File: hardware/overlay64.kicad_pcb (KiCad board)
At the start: 2 copper layers, 54 x 43.2 mm, 15 parts, among them IC1 ATMEGA328P-P, P1 ISP, P2 VIC IN, P3 VIC OUT, Q1 NPN, U1 LM1881, Y1 16MHz

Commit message: Hardware: Removed VIC-Sockets and pcb layout
Designing this as a VIC-Adpater-board is too complicated, and maybe
not possible (depending on what the modulator still does to the signal
to make it a proper C/Y signal).

It's probably simpler to get LUMA from the connector internally.
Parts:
- removed C1, C2: 18pF, Capacitors_ThroughHole:C_Disc_D3_P2.5
- removed C3, C4, C5, C6: 100nF, Capacitors_ThroughHole:C_Disc_D3_P2.5
- removed IC1: ATMEGA328P-P, Housings_DIP:DIP-28_W7.62mm
- removed P1: ISP, Pin_Headers:Pin_Header_Straight_2x03
- removed P2: VIC IN, Housings_DIP:DIP-40_W15.24mm
- removed P3: VIC OUT, Housings_DIP:DIP-40_W15.24mm
- removed Q1: NPN, TO_SOT_Packages_THT:TO-92_Inline_Narrow_Oval
- removed R1: 680k, Discret:R1
- removed RV1: 1k, Potentiometers:Potentiometer_Bourns_3339H_Angular_ScrewUp
- removed U1: LM1881, Housings_DIP:DIP-8_W7.62mm
- removed Y1: 16MHz, Crystals:Crystal_HC49-U_Vertical
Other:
- board outline removed

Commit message: Hardware: First draft of pcb layout (rough)
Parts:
- added C1: 18pF, Capacitors_ThroughHole:C_Disc_D3_P2.5, F.Cu at (135.9, 95.9)
- added C2: 18pF, Capacitors_ThroughHole:C_Disc_D3_P2.5, F.Cu at (135.9, 106.0)
- added C3: 100nF, Capacitors_ThroughHole:C_Disc_D3_P2.5, F.Cu at (141.0, 93.3)
- added C4: 100nF, Capacitors_ThroughHole:C_Disc_D3_P2.5, F.Cu at (138.4, 79.4)
- added C5: 100nF, Capacitors_ThroughHole:C_Disc_D3_P2.5, F.Cu at (132.1, 102.2)
- added C6: 100nF, Capacitors_ThroughHole:C_Disc_D3_P2.5, F.Cu at (141.0, 84.5)
- added IC1: ATMEGA328P-P, Housings_DIP:DIP-28_W7.62mm, F.Cu at (143.5, 79.4)
- added JP1: BACKDROP, Pin_Headers:Pin_Header_Straight_1x02, F.Cu at (129.5, 102.2)
- added P1: ISP, Pin_Headers:Pin_Header_Straight_2x03, F.Cu at (134.6, 112.4)
- added P2: MAIN, Pin_Headers:Pin_Header_Straight_1x03, F.Cu at (129.5, 111.1)
- added P3: INPUT/BYPASS, Pin_Headers:Pin_Header_Straight_2x14, F.Cu at (154.9, 79.4)
- added Q1: BC547B, TO_SOT_Packages_THT:TO-92_Inline_Narrow_Oval, F.Cu at (139.7, 87.0)
- added R1: 680k, Discret:R1, F.Cu at (138.4, 83.2)
- added R2: 4k7, Discret:R1, F.Cu at (135.9, 92.1)
- added RV1: 1k, Potentiometers:Potentiometer_Bourns_3339P_Angular_ScrewUp, F.Cu at (128.3, 93.3)
- added U1: LM1881, Housings_DIP:DIP-8_W7.62mm, F.Cu at (128.3, 79.4)
- added Y1: 20MHz, Crystals:Crystal_HC49-U_Vertical, F.Cu at (139.7, 101.0)
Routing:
- net GND: track 0.00 -> 76.5 mm
- net VCC: track 0.00 -> 72.4 mm
- net /IN1: track 0.00 -> 64.4 mm, vias 0 -> 1
- net /~RESET: track 0.00 -> 56.5 mm, vias 0 -> 1
- net /MOSI: track 0.00 -> 49.9 mm
- net /IN0: track 0.00 -> 44.7 mm
- net /IN8: track 0.00 -> 26.1 mm
- net /IN9: track 0.00 -> 25.8 mm
- net /IN7: track 0.00 -> 24.3 mm
- net /IN10: track 0.00 -> 24.1 mm
- net /MISO: track 0.00 -> 23.4 mm
- net /SCK: track 0.00 -> 21.9 mm
- net Net-(C5-Pad2): track 0.00 -> 20.1 mm
- net Net-(IC1-Pad4): track 0.00 -> 19.9 mm
- net Net-(JP1-Pad2): track 0.00 -> 18.8 mm
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- added copper zone on B.Cu, net GND
- added copper zone on F.Cu, net GND
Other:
- board outline added: 31.8 x 35.6 mm
- net class Default: via_dia 0.6 -> 1
- net class Power added: clearance 0.2, trace_width 0.5, via_dia 1, via_drill 0.4

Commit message: Hardware: Updated netlist to include OE/OR pins
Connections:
- IC1 pad 12: /IN12 -> /~OE
- IC1 pad 13: /~OE -> /~OR
- P3 pad 25: /IN12 -> /~OE
- P3 pad 26: /IN12 -> /~OE
- P3 pad 27: /~OE -> /~OR
- P3 pad 28: /~OE -> /~OR
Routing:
- net /IN12: track 15.0 -> 0.00 mm
- net /~OR: track 0.00 -> 15.0 mm

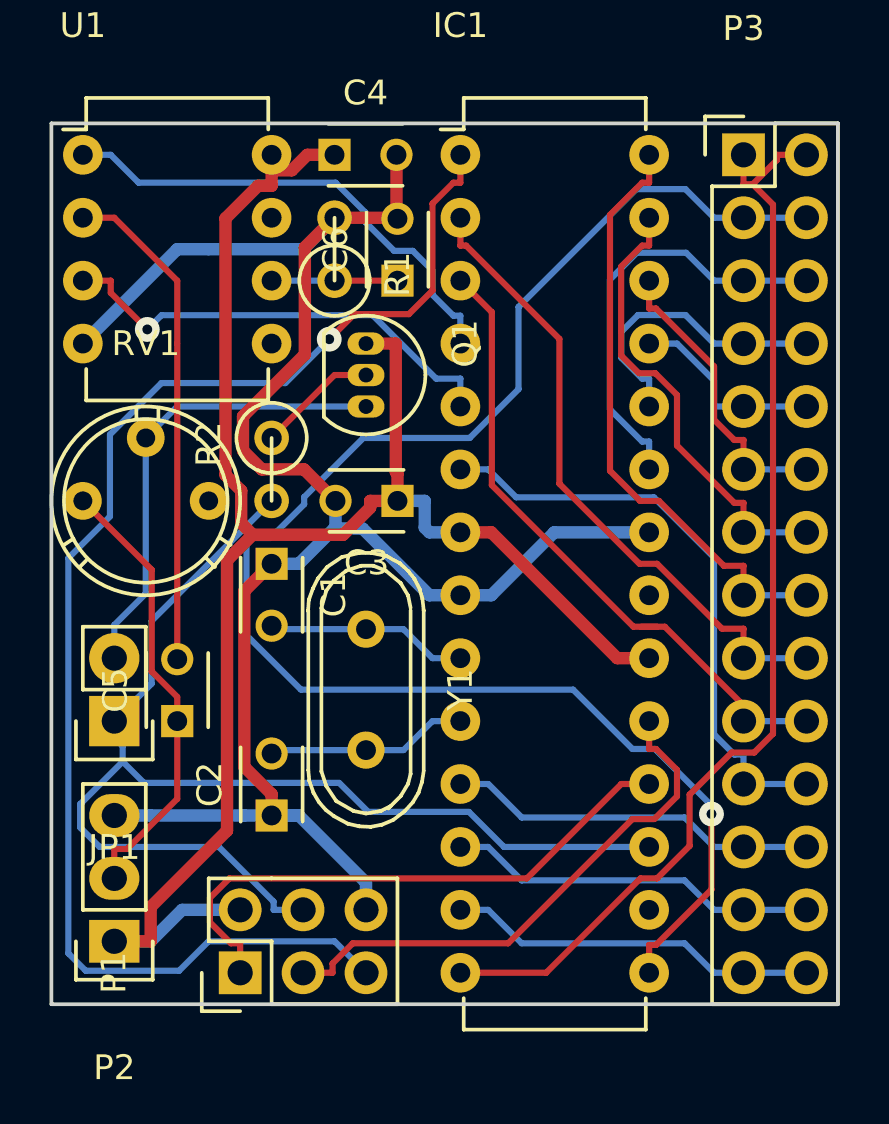
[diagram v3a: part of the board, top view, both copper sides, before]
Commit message: Hardware: Adjusted input pin connections to new logical layout
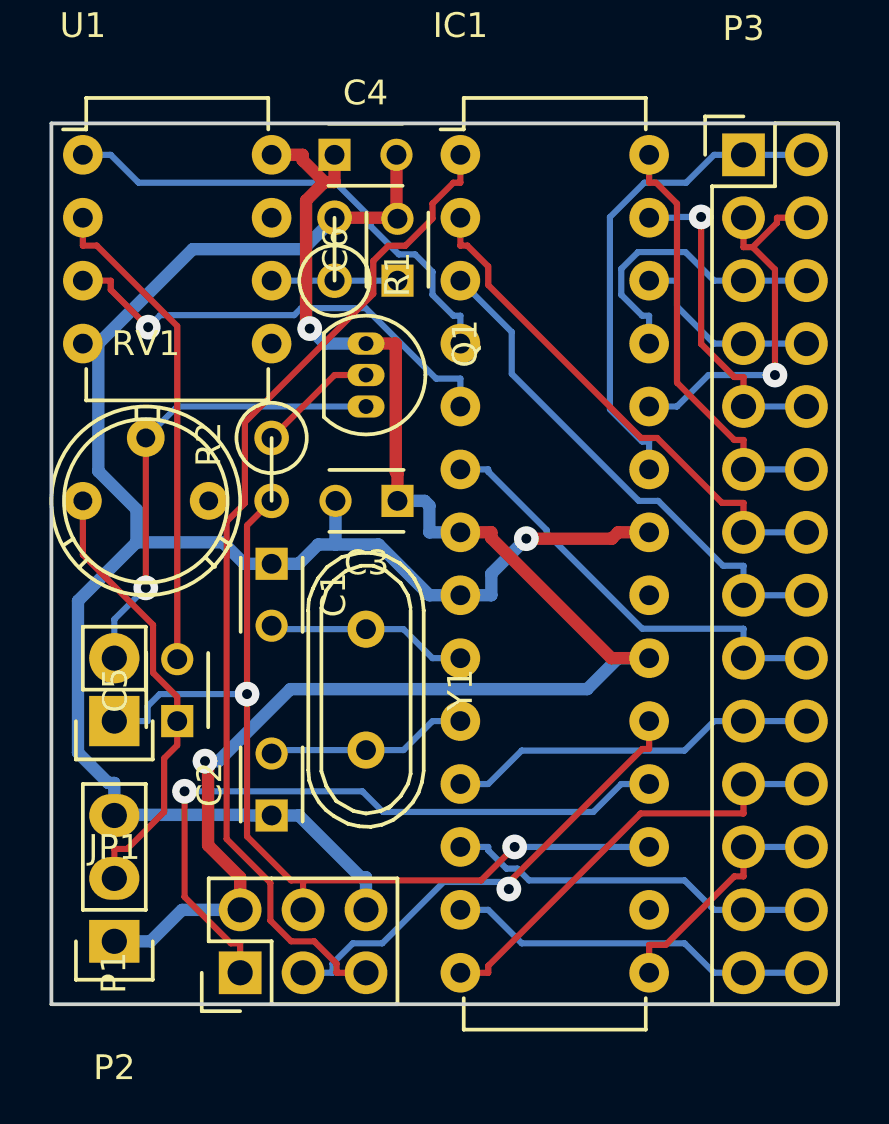
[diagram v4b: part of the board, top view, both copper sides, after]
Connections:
- IC1 pad 11: /IN11 -> /IN9
- IC1 pad 14: /IN0 -> /IN10
- IC1 pad 15: /IN1 -> /IN11
- IC1 pad 2: /IN8 -> /IN6
- IC1 pad 23: /IN2 -> /IN0
- IC1 pad 24: /IN3 -> /IN1
- IC1 pad 25: /IN4 -> /IN2
- IC1 pad 26: /IN5 -> /IN3
- IC1 pad 27: /IN6 -> /IN4
- IC1 pad 28: /IN7 -> /IN5
- IC1 pad 3: /IN9 -> /IN7
- IC1 pad 6: /IN10 -> /IN8
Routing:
- net /IN1: track 64.4 -> 15.5 mm
- net /IN0: track 44.7 -> 20.0 mm
- net /~RESET: track 56.5 -> 41.1 mm, vias 1 -> 0
- net /MOSI: track 49.9 -> 38.8 mm, vias 0 -> 2
- net /IN9: track 25.8 -> 15.0 mm
- net /IN8: track 26.1 -> 17.9 mm
- net VCC: track 72.4 -> 66.0 mm, vias 0 -> 2
- net /IN10: track 24.1 -> 18.0 mm
- net /IN2: track 17.3 -> 11.9 mm
- net /IN4: track 8.01 -> 13.2 mm, vias 0 -> 1
- net /IN11: track 15.0 -> 9.81 mm
- net /IN5: track 12.1 -> 17.2 mm
- net /MISO: track 23.4 -> 28.0 mm, vias 0 -> 1
- net /IN3: track 11.9 -> 8.01 mm
- net /IN7: track 24.3 -> 20.9 mm
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
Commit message: Hardware: Rearranged components, rerouting...
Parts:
- removed RV1: 1k, Potentiometers:Potentiometer_Bourns_3339P_Angular_ScrewUp
- added 1K: 1k, Potentiometers:Potentiometer_Bourns_3339P_Angular_ScrewUp, F.Cu at (100.3, 95.2)
- added H1: MountingHole_4mm, Mounting_Holes:MountingHole_4mm, F.Cu at (86.4, 59.7)
- added H2: MountingHole_4mm, Mounting_Holes:MountingHole_4mm, F.Cu at (115.6, 59.7)
- added H3: MountingHole_4mm, Mounting_Holes:MountingHole_4mm, F.Cu at (86.4, 101.6)
- added H4: MountingHole_4mm, Mounting_Holes:MountingHole_4mm, F.Cu at (115.6, 101.6)
- added P4: BYPASS, Pin_Headers:Pin_Header_Angled_1x12, F.Cu at (115.6, 66.7)
- added P5: INPUT, Pin_Headers:Pin_Header_Angled_1x12, F.Cu at (86.4, 94.6)
- P2: footprint Pin_Headers:Pin_Header_Straight_1x03 -> Pin_Headers:Pin_Header_Angled_1x03
- P3: value INPUT/BYPASS -> CONTROL; footprint Pin_Headers:Pin_Header_Straight_2x14 -> Pin_Headers:Pin_Header_Angled_1x02
- moved P1 65.6 mm to (94.0, 61.0)
- moved P3 50.8 mm to (109.2, 101.6), turned to 270 degrees
- moved Q1 47.6 mm to (92.1, 88.3), turned to 180 degrees
- moved C5 47.6 mm to (91.4, 77.5), turned to 180 degrees
- moved R2 46.0 mm to (90.8, 83.2), turned to 90 degrees
- moved C2 45.2 mm to (95.2, 86.4), turned to 270 degrees
- moved R1 43.6 mm to (95.2, 77.5), turned to 0 degrees
- moved Y1 43.0 mm to (99.7, 85.1)
- moved C3 42.5 mm to (101.6, 77.5)
- moved IC1 42.5 mm to (104.1, 63.5)
- moved C1 42.4 mm to (95.2, 83.8), turned to 90 degrees
- moved C6 42.2 mm to (101.0, 71.1), turned to 270 degrees
- moved U1 40.4 mm to (90.2, 66.0)
- moved JP1 39.8 mm to (90.2, 96.5)
- moved C4 39.0 mm to (101.0, 68.6), turned to 90 degrees
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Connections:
- P3 pad 1: /IN0 -> /~OE
- P3 pad 2: /IN0 -> /~OR
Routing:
- net /IN7: track 20.9 -> 91.3 mm
- net /IN4: track 13.2 -> 66.8 mm, vias 1 -> 0
- net /IN6: track 21.0 -> 67.6 mm
- net /MOSI: track 38.8 -> 82.5 mm, vias 2 -> 1
- net /IN2: track 11.9 -> 54.9 mm
- net /IN8: track 17.9 -> 57.9 mm
- net /IN9: track 15.0 -> 54.9 mm
- net /IN0: track 20.0 -> 59.4 mm
- net /IN1: track 15.5 -> 53.1 mm, vias 1 -> 0
- net /IN5: track 17.2 -> 53.6 mm
- net /IN3: track 8.01 -> 42.0 mm
- net /~RESET: track 41.1 -> 7.32 mm, vias 0 -> 1
- net /IN11: track 9.81 -> 43.4 mm
- net GND: track 76.8 -> 108.3 mm
- net /IN10: track 18.0 -> 41.2 mm
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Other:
- board size 31.8 x 35.6 mm -> 36.8 x 49.5 mm
- board text added: "1"
- board text added: "12"
- board text added: "20MHz"
- board text added: "BACKDROP"
- board text added: "BRIGHTNESS"
- board text added: "C1"
- board text added: "C2"
- board text added: "C3"
- board text added: "C4"
- board text added: "C5"
- board text added: "C6"
- board text added: "GND"
- board text added: "LUMA"
- board text added: "Overlay64 Rev.1 ©2016 Henning Bekel www.henning-bekel.de"
- board text added: "VCC"
- board text added: "~OE"
- board text added: "~OR"
